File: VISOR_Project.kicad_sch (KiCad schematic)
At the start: 30 parts, among them SW1 Short P2 to GND, SW2 Short P3 to GND, SW3 Short P6 to GND, U1 OPA170AIDBVR, U2 LM317_TO-220, U3 DRV8871DDA, U4 GD32VF103R, U5 AD8676xR, U6 MCP6002-xP

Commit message: circuit config
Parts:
- removed D1: BPW82, OptoDevice:Osram_BPW82, symbol Sensor_Optical:BPW82
- added D2: BPW82, OptoDevice:Osram_BPW82, symbol Sensor_Optical:BPW82
- added U7: STM32F103CBTx, Package_QFP:LQFP-48_7x7mm_P0.5mm, symbol MCU_ST_STM32F1:STM32F103CBTx
- C1: value 9.1p -> 8.2p
- R1: value 40.2K -> 4.22k
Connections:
- net GND: now also D2.2 (A)
- net at C1.1, R1.2, R_Extra.2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: now also Ci.1; no longer Ci.2
- net at SW1.2 (B): now also LASER1.P2 (LD-)
- net at LASER1.P3 (TUNING_Vt-): now also SW2.2 (B)
- net at LASER1.P6 (LD+/TUNING_Vt+): now also SW3.2 (B)
- new net: U7.23 (VSS), U7.35 (VSS), U7.47 (VSS)
- new net: Ci.2, D2.1 (K)
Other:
- moved on the sheet: Ci, SW1A, SW2A, SW3A

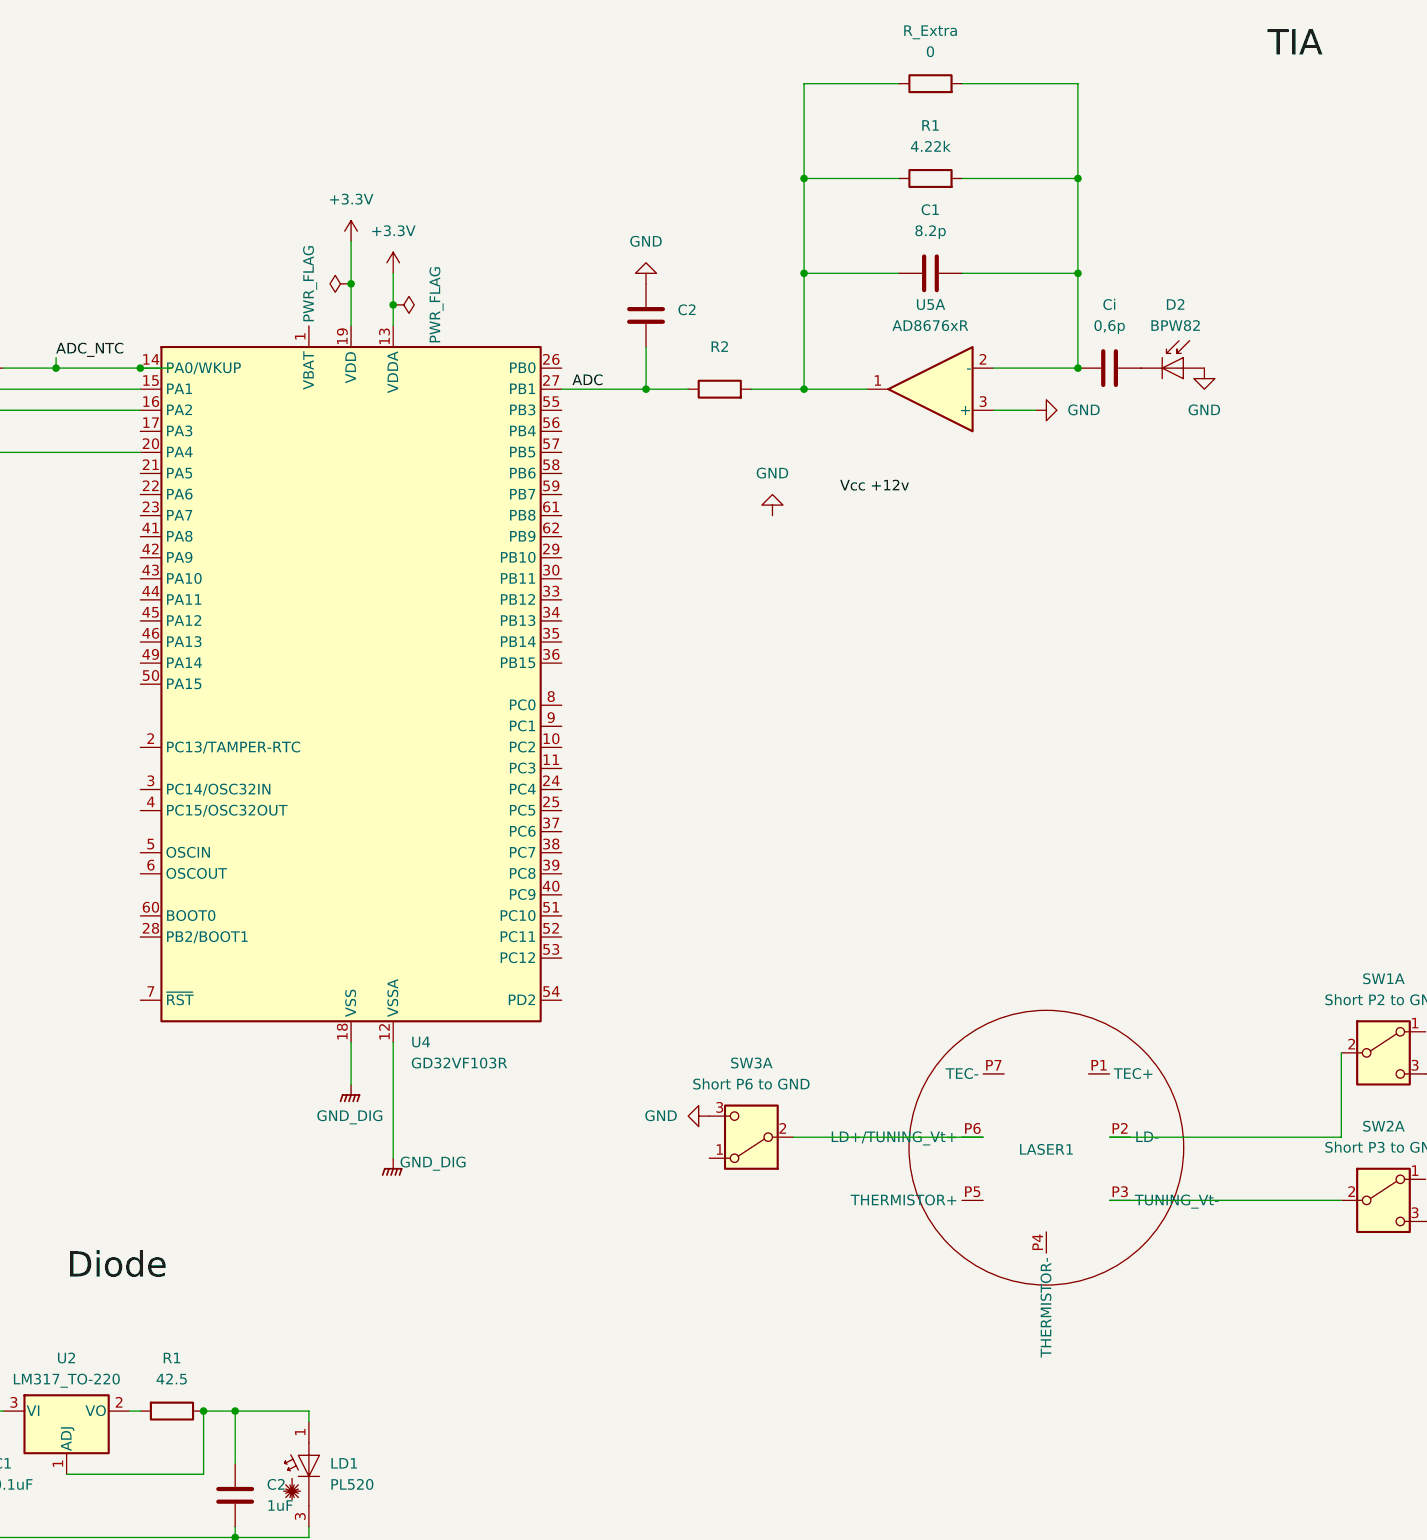
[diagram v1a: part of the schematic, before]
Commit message: TIA fix
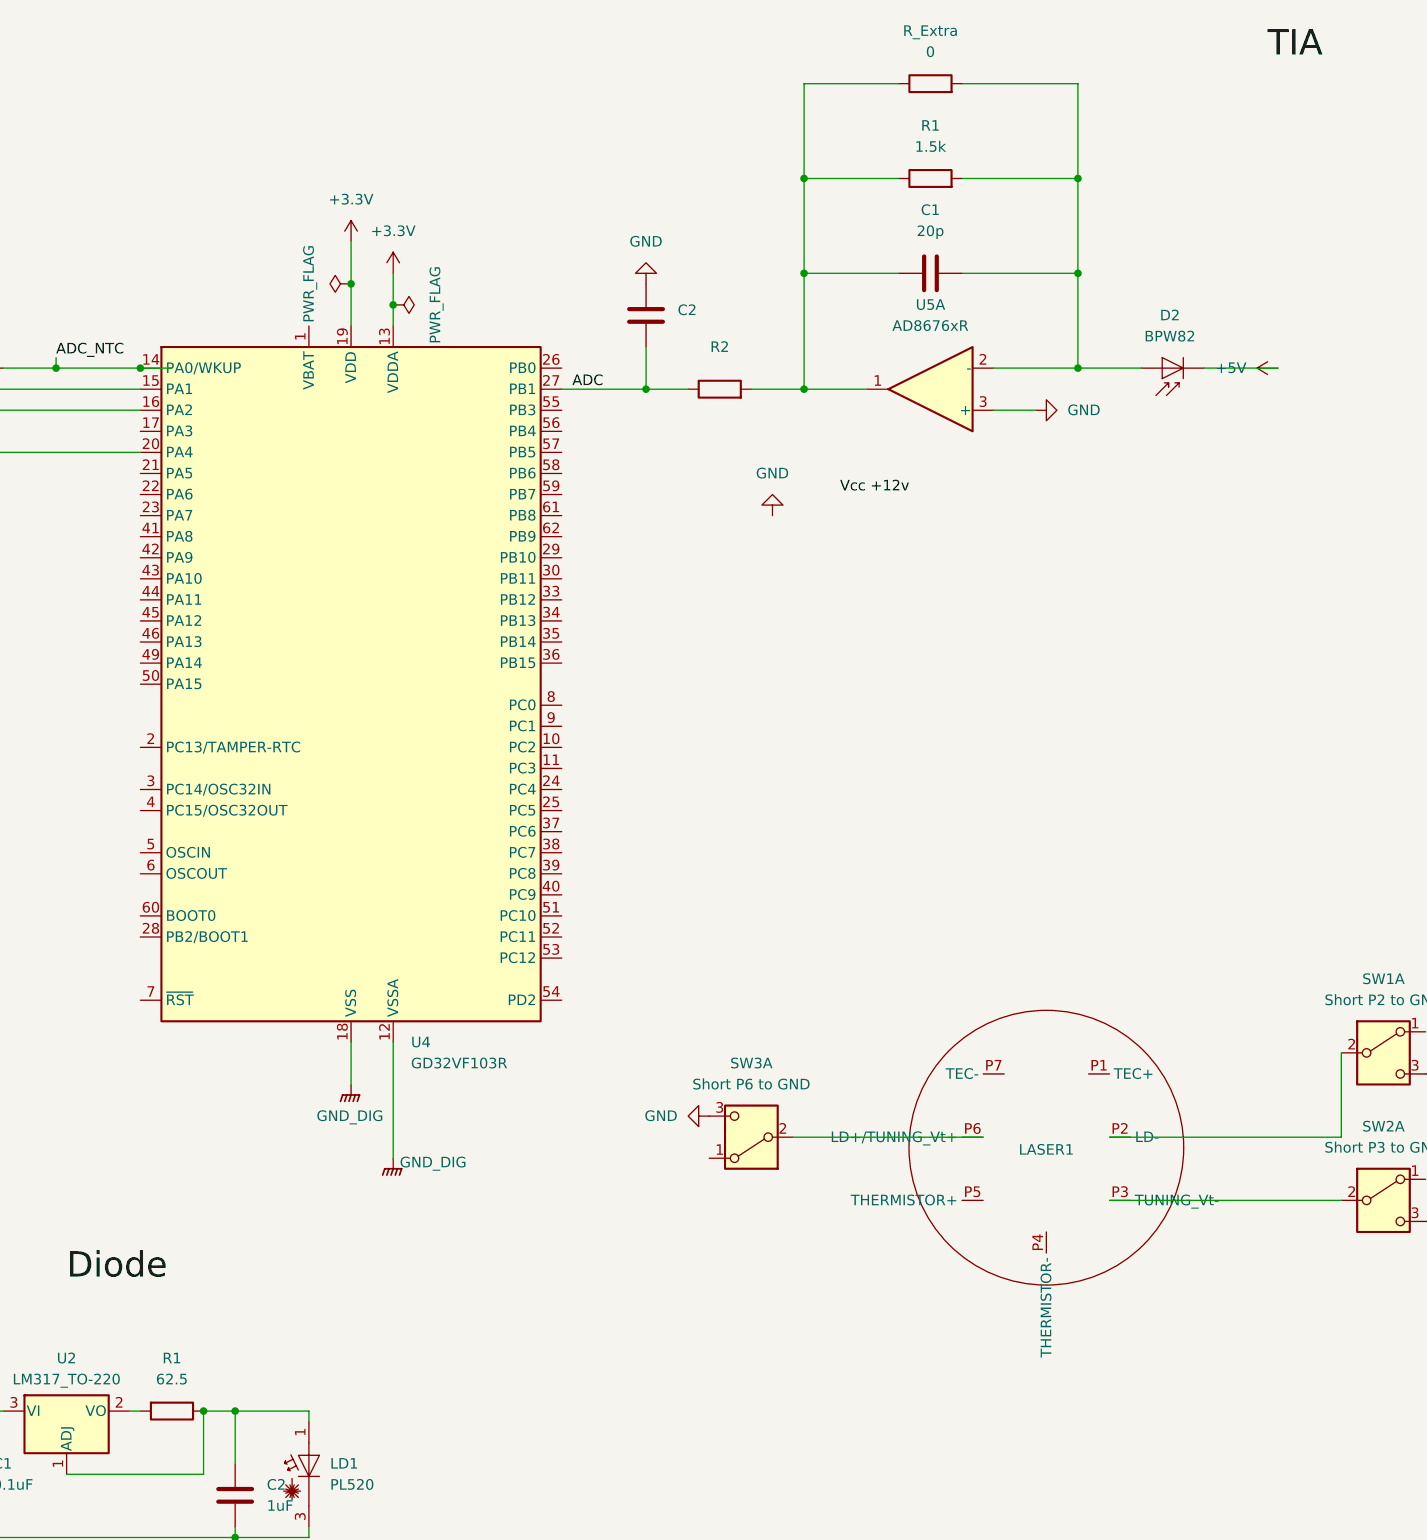
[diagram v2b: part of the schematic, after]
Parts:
- removed Ci: 0,6p, symbol Device:C
- C1: value 8.2p -> 20p
- R1: value 42.5 -> 62.5
- R1: value 4.22k -> 1.5k
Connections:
- net GND: no longer D2.2 (A)
- net +5V: now reaches D2.1 (K)
- net at C1.1, R1.2, R_Extra.2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: now also D2.2 (A)
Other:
- moved on the sheet: D2
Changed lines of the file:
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@@
 	)
 	(junction
+		(at 372.11 119.38)
+		(diameter 0)
+		(color 0 0 0 0)
+	)
+	(junction
 		(at 248.92 119.38)
 		(diameter 0)
@@
 	)
 	(junction
-		(at 372.11 119.38)
-		(diameter 0)
-		(color 0 0 0 0)
-	)
-	(junction
 		(at 289.56 111.76)
 		(diameter 0)
@@
 	(wire
 		(pts
+			(xy 372.11 119.38) (xy 379.73 119.38)
+		)
+		(stroke
+			(width 0)
+			(type default)
+		)
+	)
+	(wire
+		(pts
 			(xy 289.56 111.76) (xy 289.56 114.3)
 		)
@@
 	(wire
 		(pts
+			(xy 387.35 119.38) (xy 396.24 119.38)
+		)
+		(stroke
+			(width 0)
+			(type default)
+		)
+	)
+	(wire
+		(pts
 			(xy 266.7 245.11) (xy 270.51 245.11)
 		)
@@
 	(symbol
 		(lib_id "Sensor_Optical:BPW82")
-		(at 384.81 119.38 0)
+		(at 382.27 119.38 180)
 		(unit 1)
 		(exclude_from_sim no)
@@
 		(fields_autoplaced yes)
 		(property "Reference" "D2"
-			(at 383.8829 111.76 0)
+			(at 383.1971 113.03 0)
 			(effects
 				(font
@@
 		)
 		(property "Value" "BPW82"
-			(at 383.8829 114.3 0)
+			(at 383.1971 115.57 0)
 			(effects
 				(font
@@
 		)
 		(property "Footprint" "OptoDevice:Osram_BPW82"
-			(at 384.81 114.935 0)
+			(at 382.27 123.825 0)
 			(effects
 				(font
@@
 		)
 		(property "Description" "Silicon PIN Photodiode with Daylight Blocking Filter"
-			(at 384.81 119.38 0)
+			(at 382.27 119.38 0)
 			(effects
 				(font
@@
 			)
 		)
-		(property "Value" "42.5"
+		(property "Value" "62.5"
 			(at 262.89 241.3 90)
 			(effects
@@
 			)
 		)
-		(property "Value" "4.22k"
+		(property "Value" "1.5k"
 			(at 354.33 92.71 90)
 			(effects
@@
 			)
 		)
-		(property "Value" "8.2p"
+		(property "Value" "20p"
 			(at 354.33 102.87 90)
 			(effects
@@
 	)
 	(symbol
+		(lib_id "power:+5V")
+		(at 396.24 119.38 90)
+		(unit 1)
+		(exclude_from_sim no)
+		(in_bom yes)
+		(on_board yes)
+		(dnp no)
+		(fields_autoplaced yes)
+		(property "Reference" "#PWR018"
+			(at 400.05 119.38 0)
+			(effects
+				(font
+					(size 1.27 1.27)
+				)
+				(hide yes)
+			)
+		)
+		(property "Value" "+5V"
+			(at 392.43 119.3799 90)
+			(effects
+				(font
+					(size 1.27 1.27)
+				)
+				(justify left)
+			)
+		)
+		(property "Footprint" ""
+			(at 396.24 119.38 0)
+			(effects
+				(font
+					(size 1.27 1.27)
+				)
+				(hide yes)
+			)
+		)
+		(property "Datasheet" ""
+			(at 396.24 119.38 0)
+			(effects
+				(font
+					(size 1.27 1.27)
+				)
+				(hide yes)
+			)
+		)
+		(property "Description" "Power symbol creates a global label with name \"+5V\""
+			(at 396.24 119.38 0)
+			(effects
+				(font
+					(size 1.27 1.27)
+				)
+				(hide yes)
+			)
+		)
+		(pin "1"
+		)
+		(instances
+			(project ""
+				(path "/236c3ba3-cbc4-4020-b8ad-b2d57e4f816e"
+					(reference "#PWR018")
+					(unit 1)
+				)
+			)
+		)
+	)
+	(symbol
 		(lib_id "Regulator_Linear:LM317_TO-220")
 		(at 250.19 245.11 0)
@@
 	)
 	(symbol
-		(lib_id "Device:C")
-		(at 375.92 119.38 90)
-		(unit 1)
-		(exclude_from_sim no)
-		(in_bom yes)
-		(on_board yes)
-		(dnp no)
-		(fields_autoplaced yes)
-		(property "Reference" "Ci"
-			(at 375.92 111.76 90)
-			(effects
-				(font
-					(size 1.27 1.27)
-				)
-			)
-		)
-		(property "Value" "0,6p"
-			(at 375.92 114.3 90)
-			(effects
-				(font
-					(size 1.27 1.27)
-				)
-			)
-		)
-		(property "Footprint" ""
-			(at 379.73 118.4148 0)
-			(effects
-				(font
-					(size 1.27 1.27)
-				)
-				(hide yes)
-			)
-		)
-		(property "Datasheet" "~"
-			(at 375.92 119.38 0)
-			(effects
-				(font
-					(size 1.27 1.27)
-				)
-				(hide yes)
-			)
-		)
-		(property "Description" "Unpolarized capacitor"
-			(at 375.92 119.38 0)
-			(effects
-				(font
-					(size 1.27 1.27)
-				)
-				(hide yes)
-			)
-		)
-		(pin "2"
-		)
-		(pin "1"
-		)
-		(instances
-			(project "VISOR_Project"
-				(path "/236c3ba3-cbc4-4020-b8ad-b2d57e4f816e"
-					(reference "Ci")
-					(unit 1)
-				)
-			)
-		)
-	)
-	(symbol
 		(lib_id "power:GND")
 		(at 327.66 209.55 270)
@@
 					(unit 1)
 				)
-			)
-		)
-	)
-	(symbol
-		(lib_id "power:GND")
-		(at 387.35 119.38 0)
-		(unit 1)
-		(exclude_from_sim no)
-		(in_bom yes)
-		(on_board yes)
-		(dnp no)
-		(fields_autoplaced yes)
-		(property "Reference" "#PWR019"
-			(at 387.35 125.73 0)
-			(effects
-				(font
-					(size 1.27 1.27)
-				)
-				(hide yes)
-			)
-		)
-		(property "Value" "GND"
-			(at 387.35 124.46 0)
-			(effects
-				(font
-					(size 1.27 1.27)
-				)
-			)
-		)
-		(property "Footprint" ""
-			(at 387.35 119.38 0)
-			(effects
-				(font
-					(size 1.27 1.27)
-				)
-				(hide yes)
-			)
-		)
-		(property "Datasheet" ""
-			(at 387.35 119.38 0)
-			(effects
-				(font
-					(size 1.27 1.27)
-				)
-				(hide yes)
-			)
-		)
-		(property "Description" "Power symbol creates a global label with name \"GND\" , ground"
-			(at 387.35 119.38 0)
-			(effects
-				(font
-					(size 1.27 1.27)
-				)
-				(hide yes)
-			)
-		)
-		(pin "1"
-		)
-		(instances
-			(project "VISOR_Project"
-				(path "/236c3ba3-cbc4-4020-b8ad-b2d57e4f816e"
-					(reference "#PWR019")
-					(unit 1)
-				)

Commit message: Schematic update
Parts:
- removed D2: BPW82, OptoDevice:Osram_BPW82, symbol Sensor_Optical:BPW82
- added C5, C6: 47uF, symbol Device:C
- added L1, L2: 220uH, symbol Device:L
- added U8: ~, symbol New_Library_0:Photodiode_Module
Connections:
- net +5V: now also U8. (PD+)
- net GND: now also U8. (PD+)
- net TEC+: now also C5.2, C6.2, L2.1; no longer U3.6 (OUT1)
- net TEC-: now also C5.1, C6.1, L1.1; no longer U3.8 (OUT2)
- new net: L1.2, U3.8 (OUT2)
- new net: L2.2, U3.6 (OUT1)

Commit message: Schematic update
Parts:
- removed U5: AD8676xR, Package_SO:SOIC-8_3.9x4.9mm_P1.27mm, symbol Amplifier_Operational:AD8676xR
- removed U7: STM32F103CBTx, Package_QFP:LQFP-48_7x7mm_P0.5mm, symbol MCU_ST_STM32F1:STM32F103CBTx
- added U5: MCP6002-I_P, Promix_Lib:DIP787W46P254L927H533Q8, symbol MCP6002-I_P:MCP6002-I_P
- C8: renamed from C1; footprint (none) -> Capacitor_THT:C_Disc_D5.1mm_W3.2mm_P5.00mm
- LASER1: footprint (none) -> Promix_Lib:Las_Socket
- LP_C_TIA1: renamed from C2; footprint (none) -> Capacitor_THT:C_Disc_D5.1mm_W3.2mm_P5.00mm
- LP_R_TIA1: renamed from R2; footprint (none) -> Resistor_THT:R_Axial_DIN0207_L6.3mm_D2.5mm_P2.54mm_Vertical
- R8: renamed from R1; footprint (none) -> Resistor_THT:R_Axial_DIN0207_L6.3mm_D2.5mm_P2.54mm_Vertical
- R_Extra1: renamed from R_Extra; footprint (none) -> Resistor_THT:R_Axial_DIN0207_L6.3mm_D2.5mm_P2.54mm_Vertical
- U6: renamed from U8; footprint (none) -> Promix_Lib:INGaAS_Photodiode
- renumbered C5 to C1, C6 to C2, C1 to C5, C2 to C6, R5 to R1, R6 to R2, R9 to R3, R3 to R4, R4 to R5, R1 to R6, SW3 to SW1, SW1 to SW2, SW2 to SW3, U3 to U1, U6 to U2, U2 to U3, U1 to U7
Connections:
- net +5V: now also U6.2 (PD-), U5.8 (VDD); no longer U6. (PD+)
- net GND: now also U6.1 (CASE), U5.5 (VINB+); no longer U6. (PD+)
- net at C8.2, LP_R_TIA1.2, R8.1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: now also U5.7 (VOUTB)
- net at C8.1, R8.2, R_Extra1.2: now also U6.3 (PD+), U5.6 (VINB-)
- new net V- V: U5.4 (VSS)
